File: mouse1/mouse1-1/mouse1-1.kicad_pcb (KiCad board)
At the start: 2 copper layers, 38 x 65.5 mm, 17 parts

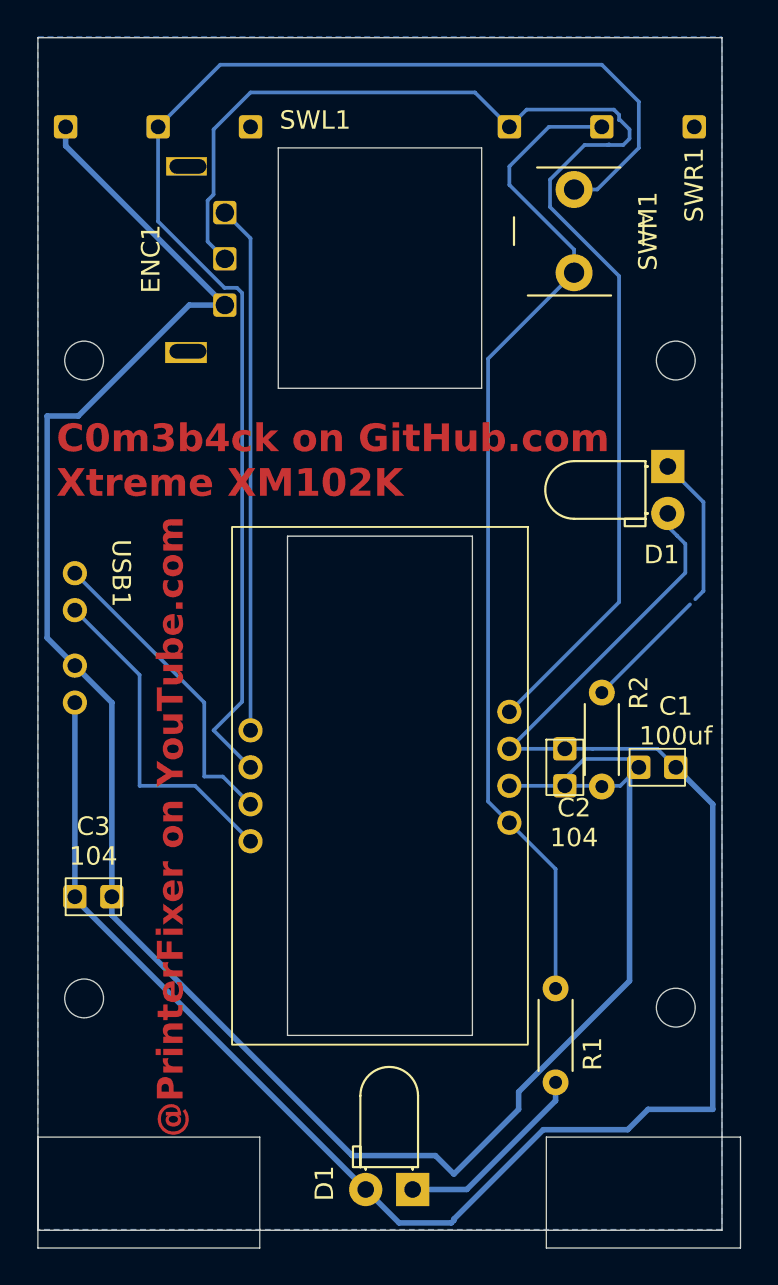
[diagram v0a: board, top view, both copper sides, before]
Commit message: Finished PCB - added full labels and all components, even if not actually soldered
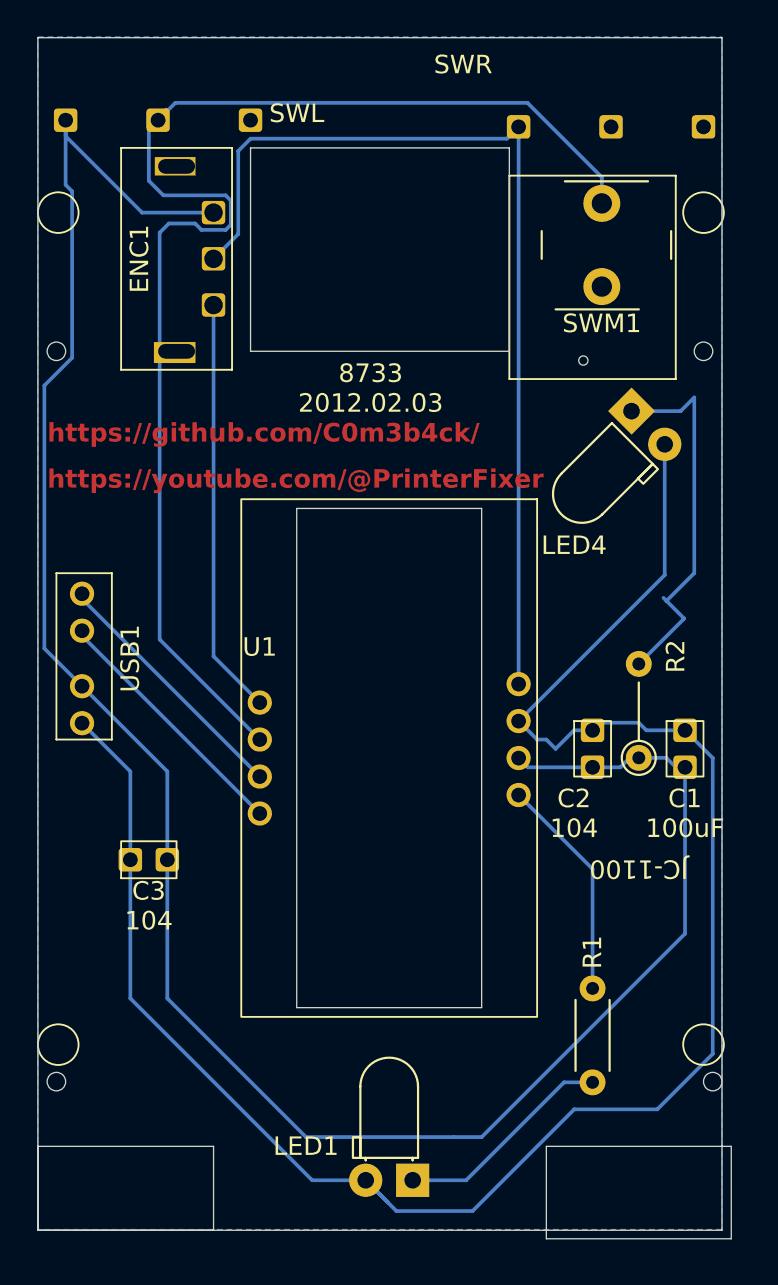
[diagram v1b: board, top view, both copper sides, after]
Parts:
- removed D1 (x2): LED, LED_THT:LED_D3.0mm_Horizontal_O1.27mm_Z2.0mm
- removed the REF** at (165.5, 63.5)
- removed the REF** at (166.5, 76.5)
- removed the REF** at (166.5, 41.5)
- removed the REF** at (134.5, 41.5)
- removed the REF** at (134.5, 76.0)
- removed the REF** at (135.0, 70.5)
- removed SWL1, SWR1: ~, D2FT:D2FT_SW
- added C1: ~, SmallCapacitor:SmallCapacitor, F.Cu at (162.0, 62.5)
- added C3: ~, SmallCapacitor:SmallCapacitor, F.Cu at (138.0, 68.5)
- added D2: VCC_LED, LED_THT:LED_D3.0mm_Horizontal_O1.27mm_Z2.0mm, F.Cu at (164.1, 44.2)
- added LED1: LED, LED_THT:LED_D3.0mm_Horizontal_O1.27mm_Z2.0mm, F.Cu at (152.3, 85.8)
- added REF**: MountingHole_2.1mm, MountingHole-NoMarks:MountingHole_2.1mm, F.Cu at (168.0, 41.0)
- added REF**: MountingHole_2.1mm, MountingHole-NoMarks:MountingHole_2.1mm, F.Cu at (133.0, 41.0)
- added REF**: MountingHole_2.1mm, MountingHole-NoMarks:MountingHole_2.1mm, F.Cu at (133.0, 80.5)
- added REF**: MountingHole_2.1mm, MountingHole-NoMarks:MountingHole_2.1mm, F.Cu at (168.5, 80.5)
- added REF**: MountingHole_2.1mm, MountingHole-NoMarks:MountingHole_2.1mm, F.Cu at (161.5, 41.5)
- added SWL: ~, D2FT:D2FT_SW, F.Cu at (137.5, 24.0)
- added SWR: ~, D2FT:D2FT_SW, F.Cu at (162.0, 24.4)
- C2: value SmallCapacitor -> ~
- R2: value 100 ohm -> R; footprint Resistor_THT:R_Axial_DIN0204_L3.6mm_D1.6mm_P5.08mm_Horizontal -> Resistor_THT:R_Axial_DIN0204_L3.6mm_D1.6mm_P5.08mm_Vertical
- SWM1: footprint SW_PUSH_6mm_h7.3mm-2pin:SW_PUSH_6mm_h7.3mm -> 2pin_btn:SW_PUSH_6mm_h7.3mm
- moved C2 6.58 mm to (167.0, 62.5)
- moved R2 2.53 mm to (164.5, 63.0)
- moved R1 2.00 mm to (162.0, 75.5)
- moved SWM1 1.68 mm to (159.5, 33.0)
- moved U1 1.58 mm to (144.5, 60.0)
- moved USB1 1.18 mm to (135.9, 53.1)
- moved ENC1 0.61 mm to (136.5, 41.5)
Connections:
- C2 pad 1: (no net) -> Net-(C1-GND)
- C2 pad 2: (no net) -> Net-(C1-VCC)
- ENC1 pad 1: Net-(ENC1-A) -> Net-(ENC1-C)
- ENC1 pad 3: Net-(ENC1-C) -> Net-(C1-GND)
- R2 pad 1: Net-(R2-Pad1) -> Net-(C1-GND)
- R2 pad 2: Net-(R2-Pad2) -> Net-(C1-GND)
- U1 pad 6: Net-(ENC1-A) -> Net-(C1-VCC)
- U1 pad 7: Net-(D1-A) -> Net-(C1-GND)
- USB1 pad 3: Net-(ENC1-A) -> Net-(C1-VCC)
- USB1 pad 4: Net-(D1-A) -> Net-(C1-GND)
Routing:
- net Net-(C1-GND): track 0.00 -> 136.4 mm
- net Net-(R2-Pad1): track 114.9 -> 0.00 mm
- net Net-(C1-VCC): track 0.00 -> 105.5 mm
- net Net-(D1-A): track 101.2 -> 0.00 mm
- net Net-(SWR1-NO): track 55.7 -> 12.1 mm
- net Net-(ENC1-B): track 72.7 -> 52.6 mm
- net (no net): track 8.16 -> 0.00 mm
- net Net-(R2-Pad2): track 6.75 -> 0.00 mm
- net Net-(ENC1-C): track 28.6 -> 23.0 mm
- net Net-(U1-DM): track 18.2 -> 13.9 mm
- net Net-(U1-DP): track 17.5 -> 13.9 mm
- net Net-(D1-K): track 10.7 -> 12.2 mm
- net Net-(SWL1-NO): track 73.5 -> 72.4 mm
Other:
- board size 38 x 65.5 mm -> 37.5 x 65 mm
- board text added: "8733 2012.02.03"
- board text added: "C1 100uF"
- board text added: "JC-1100"
- board text added: "LED4"
- board text added: "U1"
- board text added: "https://github.com/C0m3b4ck/"
- board text added: "https://youtube.com/@PrinterFixer"
- board text removed: "@PrinterFixer on YouTube.com"
- board text removed: "C0m3b4ck on GitHub.com Xtreme XM102K"
- board text removed: "C1 100uf"

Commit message: Updated underside and top PCB photos, updated SWM position and some connections on PCB, updated GERBER file
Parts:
- moved SWM1 1.77 mm to (157.8, 33.2)
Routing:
- net Net-(SWR1-NO): track 12.1 -> 52.3 mm
- net Net-(SWL1-NO): track 72.4 -> 73.4 mm
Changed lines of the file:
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@@
 	(footprint "2pin_btn:SW_PUSH_6mm_h7.3mm"
 		(layer "F.Cu")
-		(at 159.5 33)
+		(at 157.75 33.25)
 		(descr "tactile push button, 6x6mm e.g. PHAP33xx series, height=7.3mm")
 		(tags "tact sw push 6mm")
@@
 	)
 	(segment
-		(start 162.5 33)
-		(end 162.5 31.585787)
-		(width 0.2)
-		(layer "B.Cu")
-		(net "Net-(SWL1-NO)")
-	)
-	(segment
 		(start 142.435 34.15295)
 		(end 142.15295 34.435)
@@
 	(segment
 		(start 162.5 31.585787)
-		(end 158.479213 27.565)
+		(end 162.457106 31.542894)
 		(width 0.2)
 		(layer "B.Cu")
@@
 	)
 	(segment
+		(start 162.457106 31.542894)
+		(end 160.75 33.25)
+		(width 0.2)
+		(layer "B.Cu")
+		(net "Net-(SWL1-NO)")
+	)
+	(segment
 		(start 138 31.776364)
 		(end 138 29)
@@
 	)
 	(segment
+		(start 162.457106 31.542894)
+		(end 158.479213 27.565)
+		(width 0.2)
+		(layer "B.Cu")
+		(net "Net-(SWL1-NO)")
+	)
+	(segment
 		(start 158.479213 27.565)
 		(end 139.435 27.565)
@@
 	)
 	(segment
+		(start 160.75 37.75)
+		(end 161 37.5)
+		(width 0.2)
+		(layer "F.Cu")
+		(net "Net-(SWR1-NO)")
+	)
+	(segment
+		(start 157.60484 59.954)
+		(end 158.39516 59.954)
+		(width 0.2)
+		(layer "B.Cu")
+		(net "Net-(SWR1-NO)")
+	)
+	(segment
 		(start 158 65)
 		(end 162 69)
@@
 	)
 	(segment
+		(start 163 35.5)
+		(end 163 28.8625)
+		(width 0.2)
+		(layer "B.Cu")
+		(net "Net-(SWR1-NO)")
+	)
+	(segment
+		(start 160.75 37.75)
+		(end 161 38)
+		(width 0.2)
+		(layer "B.Cu")
+		(net "Net-(SWR1-NO)")
+	)
+	(segment
+		(start 157.046 60.51284)
+		(end 157.60484 59.954)
+		(width 0.2)
+		(layer "B.Cu")
+		(net "Net-(SWR1-NO)")
+	)
+	(segment
+		(start 157.046 64.046)
+		(end 157.046 60.51284)
+		(width 0.2)
+		(layer "B.Cu")
+		(net "Net-(SWR1-NO)")
+	)
+	(segment
+		(start 160.75 37.75)
+		(end 163 35.5)
+		(width 0.2)
+		(layer "B.Cu")
+		(net "Net-(SWR1-NO)")
+	)
+	(segment
 		(start 162 69)
 		(end 162 75.46)
 		(width 0.2)
 		(layer "B.Cu")
+		(net "Net-(SWR1-NO)")
+	)
+	(segment
+		(start 158.39516 59.954)
+		(end 160.75 57.59916)
+		(width 0.2)
+		(layer "B.Cu")
+		(net "Net-(SWR1-NO)")
+	)
+	(segment
+		(start 160.75 57.59916)
+		(end 160.75 37.75)
+		(width 0.2)
+		(layer "B.Cu")
+		(net "Net-(SWR1-NO)")
+	)
+	(segment
+		(start 158 65)
+		(end 157.046 64.046)
+		(width 0.2)
+		(layer "B.Cu")
